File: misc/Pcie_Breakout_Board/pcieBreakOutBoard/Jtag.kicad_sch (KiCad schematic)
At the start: 6 parts, among them U1 FT2232HL, U3 93LCxxBxxOT

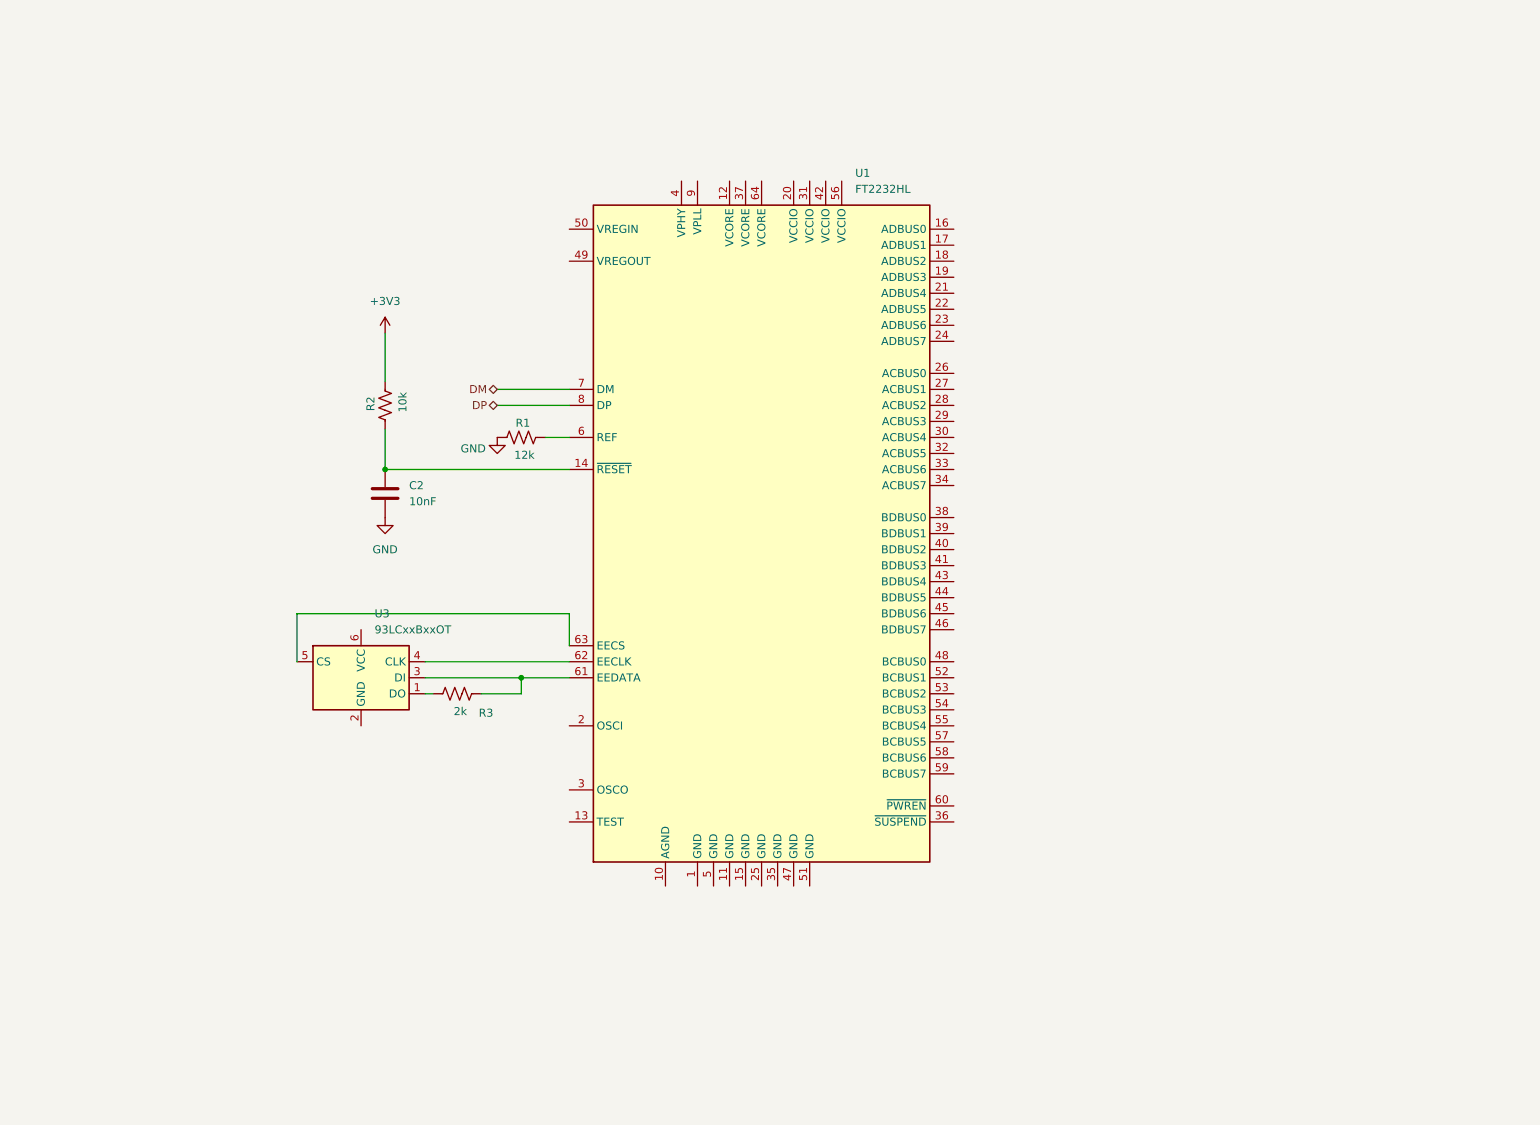
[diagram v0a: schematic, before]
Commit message: Jtag
Added jtag and serial interface to the breakout board
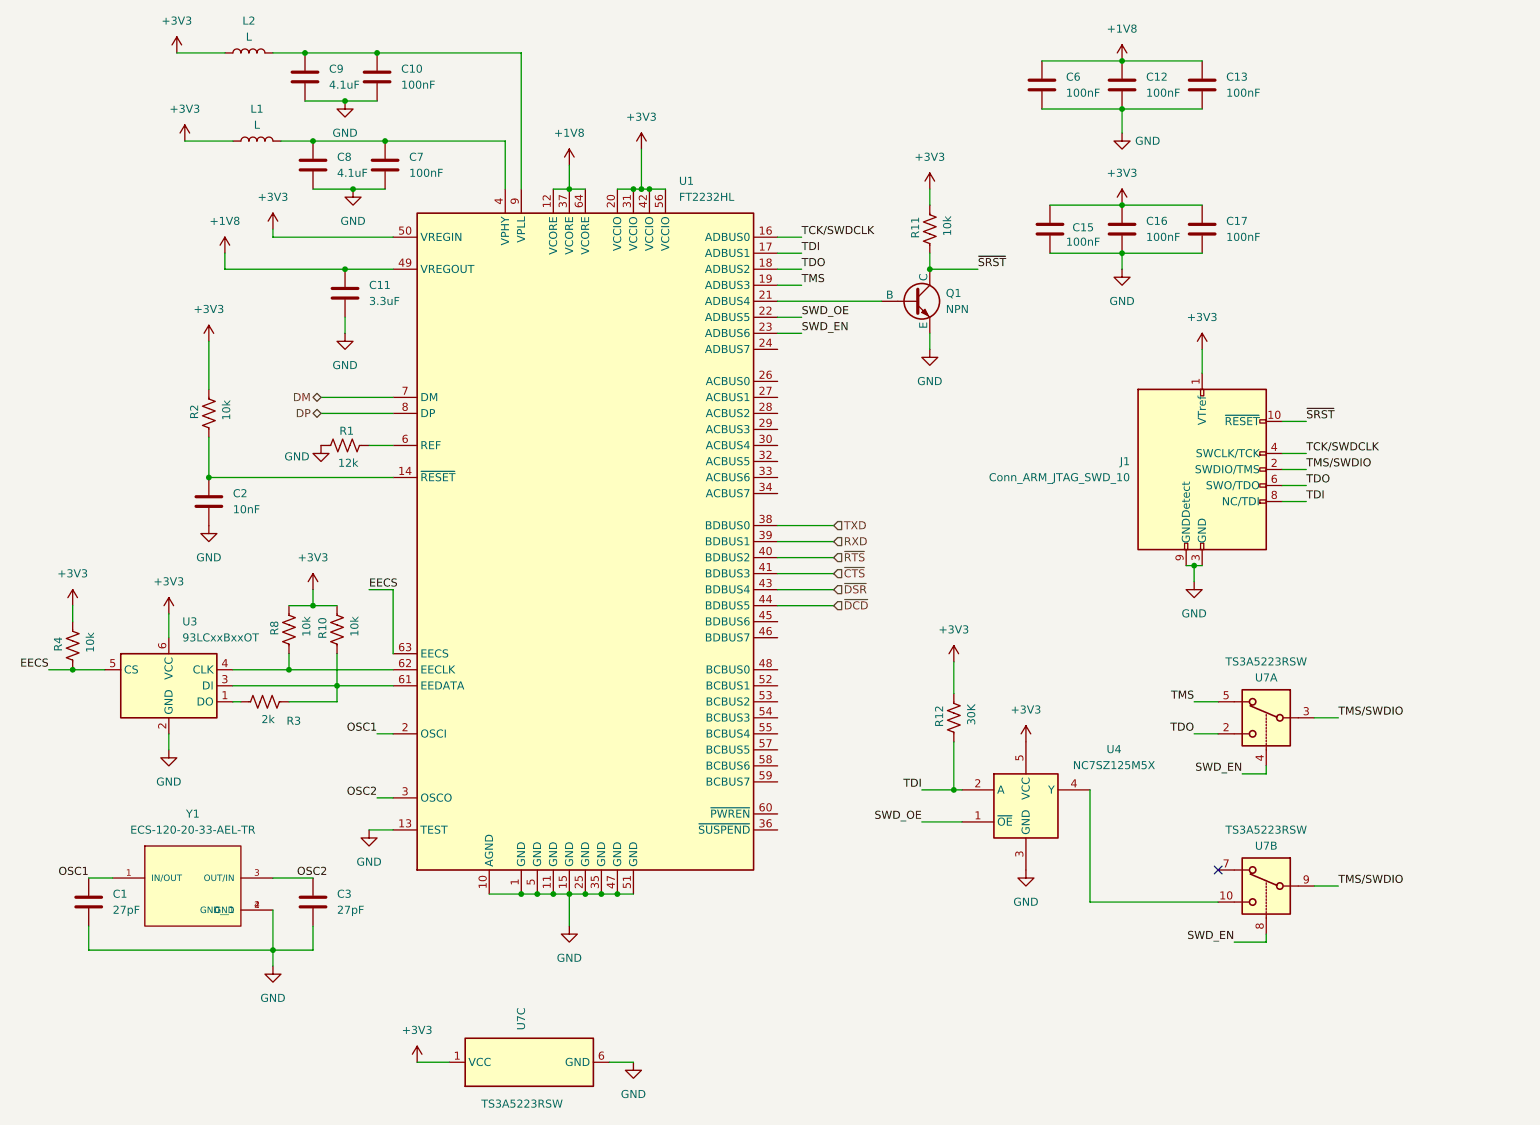
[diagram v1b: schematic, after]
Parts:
- added C1, C3: 27pF, Capacitor_SMD:C_0402_1005Metric_Pad0.74x0.62mm_HandSolder, symbol Device:C
- added C10, C12, C13, C15, C16, C17, C6, C7: 100nF, Capacitor_SMD:C_0402_1005Metric_Pad0.74x0.62mm_HandSolder, symbol Device:C
- added C11: 3.3uF, Capacitor_SMD:C_0402_1005Metric_Pad0.74x0.62mm_HandSolder, symbol Device:C
- added C8, C9: 4.1uF, Capacitor_SMD:C_0402_1005Metric_Pad0.74x0.62mm_HandSolder, symbol Device:C
- added J1: Conn_ARM_JTAG_SWD_10, Connector_PinHeader_1.27mm:PinHeader_2x05_P1.27mm_Vertical, symbol Connector:Conn_ARM_JTAG_SWD_10
- added L1, L2: L, Inductor_SMD:L_0402_1005Metric_Pad0.77x0.64mm_HandSolder, symbol Device:L
- added Q1: NPN, symbol Simulation_SPICE:NPN
- added R10, R11, R4, R8: 10k, Resistor_SMD:R_0402_1005Metric_Pad0.72x0.64mm_HandSolder, symbol Device:R_US
- added R12: 30K, Resistor_SMD:R_0402_1005Metric_Pad0.72x0.64mm_HandSolder, symbol Device:R_US
- added U4: NC7SZ125M5X, Package_TO_SOT_SMD:SOT-23-5, symbol 74xGxx:NC7SZ125M5X
- added U7: TS3A5223RSW, Package_DFN_QFN:Texas_RSW0010A_UQFN-10_1.4x1.8mm_P0.4mm, symbol Analog_Switch:TS3A5223RSW
- added Y1: ECS-120-20-33-AEL-TR, User_Footprint:XTAL_ECS-120-20-33-AEL-TR, symbol _Misc_Symbols:ECS-120-20-33-AEL-TR
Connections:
- net +3V3: now also U1.20 (VCCIO), U1.31 (VCCIO), U1.42 (VCCIO), U1.50 (VREGIN), U1.56 (VCCIO), U3.6 (VCC), C15.1, C16.1, C17.1, J1.1 (VTref), L1.1, L2.1, R10.2, R11.2, R12.2, R4.2, R8.2, U4.5 (VCC), U7.1 (VCC)
- net GND: now also U1.1 (GND), U1.10 (AGND), U1.11 (GND), U1.13 (TEST), U1.15 (GND), U1.25 (GND), U1.35 (GND), U1.47 (GND), U1.5 (GND), U1.51 (GND), U3.2 (GND), C1.2, C10.2, C11.2, C12.2, C13.2, C15.2, C16.2, C17.2, C3.2, C6.2, C7.2, C8.2, C9.2, J1.3 (GND), J1.5 (GND), J1.9 (GNDDetect), Q1.3 (E), U4.3 (GND), U7.6 (GND), Y1.2 (GND), Y1.4 (GND__1)
- net at R3.2, U1.61 (EEDATA), U3.3 (DI): now also R10.1
- net at U1.62 (EECLK), U3.4 (CLK): now also R8.1
- net EECS: now reaches U1.63 (EECS), U3.5 (CS)
- net EECS: now also R4.1
- net +1V8: now reaches U1.12 (VCORE)
- net +1V8: now also U1.37 (VCORE), U1.49 (VREGOUT), U1.64 (VCORE), C11.1, C12.1, C13.1, C6.1
- net TCK/SWDCLK: now reaches U1.16 (ADBUS0)
- net TCK/SWDCLK: now also J1.4 (SWCLK/TCK)
- net TDI: now reaches U1.17 (ADBUS1)
- net TDI: now also J1.8 (NC/TDI), R12.1, U4.2 (A)
- net TDO: now reaches U1.18 (ADBUS2)
- net TDO: now also J1.6 (SWO/TDO), U7.2
- net TMS: now reaches U1.19 (ADBUS3)
- net TMS: now also U7.5
- net OSC1: now reaches U1.2 (OSCI)
- net OSC1: now also C1.1, Y1.1 (IN/OUT)
- net at U1.21 (ADBUS4): now also Q1.2 (B)
- net SWD_OE: now reaches U1.22 (ADBUS5)
- net SWD_OE: now also U4.1 (~{OE})
- net SWD_EN: now reaches U1.23 (ADBUS6)
- net SWD_EN: now also U7.4, U7.8
- net OSC2: now reaches U1.3 (OSCO)
- net OSC2: now also C3.1, Y1.3 (OUT/IN)
- net TXD: now reaches U1.38 (BDBUS0)
- net RXD: now reaches U1.39 (BDBUS1)
- net at U1.4 (VPHY): now also C7.1, C8.1, L1.2
- net ~{RTS}: now reaches U1.40 (BDBUS2)
- net ~{CTS}: now reaches U1.41 (BDBUS3)
- net ~{DSR}: now reaches U1.43 (BDBUS4)
- net ~{DCD}: now reaches U1.44 (BDBUS5)
- net at U1.9 (VPLL): now also C10.1, C9.1, L2.2
- new net: U4.4 (Y), U7.10
- new net TMS/SWDIO: J1.2 (SWDIO/TMS), U7.3, U7.9
- new net ~{SRST}: J1.10 (~{RESET}), Q1.1 (C), R11.1
- no-connect marks 0 -> 1
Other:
- moved on the sheet: C2, R1, R2, R3, U1, U3

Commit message: routing
Start routing of the jtag part
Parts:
- removed Q1: NPN, symbol Simulation_SPICE:NPN
- added Q1: MMBT2222A, Package_TO_SOT_SMD:SOT-23_Handsoldering, symbol Transistor_BJT:MMBT2222A
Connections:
- net GND: now also Q1.2 (E)
- net OSC1: now also C3.1, Y1.3 (OUT/IN); no longer C1.1, Y1.1 (IN/OUT)
- net OSC2: now also C1.1, Y1.1 (IN/OUT); no longer C3.1, Y1.3 (OUT/IN)
- net ~{SRST}: now also Q1.3 (C)
- net at U1.21 (ADBUS4): now also Q1.1 (B)
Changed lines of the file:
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@@
 	)
 	(junction
-		(at 175.26 55.88)
-		(diameter 0)
-		(color 0 0 0 0)
-	)
-	(junction
 		(at 77.47 109.22)
 		(diameter 0)
@@
 	)
 	(junction
+		(at 175.26 55.88)
+		(diameter 0)
+		(color 0 0 0 0)
+	)
+	(junction
 		(at 179.07 138.43)
 		(diameter 0)
@@
 	)
 	(label "OSC2"
-		(at 74.93 152.4 0)
+		(at 41.91 152.4 0)
 		(effects
 			(font
@@
 	)
 	(label "OSC1"
-		(at 41.91 152.4 180)
+		(at 77.47 152.4 180)
 		(effects
 			(font
@@
 	)
 	(symbol
-		(lib_id "Simulation_SPICE:NPN")
-		(at 172.72 60.96 0)
-		(unit 1)
-		(exclude_from_sim no)
-		(in_bom yes)
-		(on_board yes)
-		(dnp no)
-		(fields_autoplaced yes)
-		(property "Reference" "Q1"
-			(at 177.8 59.6899 0)
-			(effects
-				(font
-					(size 1.27 1.27)
-				)
-				(justify left)
-			)
-		)
-		(property "Value" "NPN"
-			(at 177.8 62.2299 0)
-			(effects
-				(font
-					(size 1.27 1.27)
-				)
-				(justify left)
-			)
-		)
-		(property "Footprint" ""
-			(at 236.22 60.96 0)
-			(effects
-				(font
-					(size 1.27 1.27)
-				)
-				(hide yes)
-			)
-		)
-		(property "Datasheet" "https://ngspice.sourceforge.io/docs/ngspice-html-manual/manual.xhtml#cha_BJTs"
-			(at 236.22 60.96 0)
-			(effects
-				(font
-					(size 1.27 1.27)
-				)
-				(hide yes)
-			)
-		)
-		(property "Description" "Bipolar transistor symbol for simulation only, substrate tied to the emitter"
-			(at 172.72 60.96 0)
-			(effects
-				(font
-					(size 1.27 1.27)
-				)
-				(hide yes)
-			)
-		)
-		(property "Sim.Device" "NPN"
-			(at 172.72 60.96 0)
-			(effects
-				(font
-					(size 1.27 1.27)
-				)
-				(hide yes)
-			)
-		)
-		(property "Sim.Type" "GUMMELPOON"
-			(at 172.72 60.96 0)
-			(effects
-				(font
-					(size 1.27 1.27)
-				)
-				(hide yes)
-			)
-		)
-		(property "Sim.Pins" "1=C 2=B 3=E"
-			(at 172.72 60.96 0)
-			(effects
-				(font
-					(size 1.27 1.27)
-				)
-				(hide yes)
-			)
-		)
-		(pin "1"
-		)
-		(pin "2"
-		)
-		(pin "3"
-		)
-		(instances
-			(project "pcieBreakOutBoard"
-				(path "/12b1338c-66b4-40fc-bcb6-22ba3c1b4efc/a6f2494a-799a-42fc-83bb-1a352a63812f"
-					(reference "Q1")
-					(unit 1)
-				)
-			)
-		)
-	)
-	(symbol
 		(lib_id "Device:R_US")
 		(at 60.96 78.74 180)
@@
 					(unit 1)
 				)
+			)
+		)
+	)
+	(symbol
+		(lib_id "Transistor_BJT:MMBT2222A")
+		(at 172.72 60.96 0)
+		(unit 1)
+		(exclude_from_sim no)
+		(in_bom yes)
+		(on_board yes)
+		(dnp no)
+		(fields_autoplaced yes)
+		(property "Reference" "Q1"
+			(at 177.8 59.6899 0)
+			(effects
+				(font
+					(size 1.27 1.27)
+				)
+				(justify left)
+			)
+		)
+		(property "Value" "MMBT2222A"
+			(at 177.8 62.2299 0)
+			(effects
+				(font
+					(size 1.27 1.27)
+				)
+				(justify left)
+			)
+		)
+		(property "Footprint" "Package_TO_SOT_SMD:SOT-23_Handsoldering"
+			(at 177.8 62.865 0)
+			(effects
+				(font
+					(size 1.27 1.27)
+					(italic yes)
+				)
+				(justify left)
+				(hide yes)
+			)
+		)
+		(property "Datasheet" "https://assets.nexperia.com/documents/data-sheet/MMBT2222A.pdf"
+			(at 172.72 60.96 0)
+			(effects
+				(font
+					(size 1.27 1.27)
+				)
+				(justify left)
+				(hide yes)
+			)
+		)
+		(property "Description" "600mA Ic, 40V Vce, NPN Transistor, SOT-23"
+			(at 172.72 60.96 0)
+			(effects
+				(font
+					(size 1.27 1.27)
+				)
+				(hide yes)
+			)
+		)
+		(property "Sim.Device" "NPN"
+			(at 172.72 60.96 0)
+			(effects
+				(font
+					(size 1.27 1.27)
+				)
+				(hide yes)
+			)
+		)
+		(property "Sim.Pins" "1=B 2=E 3=C"
+			(at 172.72 60.96 0)
+			(effects
+				(font
+					(size 1.27 1.27)
+				)
+				(hide yes)
+			)
+		)
+		(pin "2"
+		)
+		(pin "3"
+		)
+		(pin "1"
+		)
+		(instances
+			(project "pcieBreakOutBoard"
+				(path "/12b1338c-66b4-40fc-bcb6-22ba3c1b4efc/a6f2494a-799a-42fc-83bb-1a352a63812f"
+					(reference "Q1")
+					(unit 1)
+				)

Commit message: layout
finished 70% of layout
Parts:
- added J4: Conn_02x04_Odd_Even, Connector_PinHeader_2.54mm:PinHeader_2x04_P2.54mm_Vertical, symbol Connector_Generic:Conn_02x04_Odd_Even
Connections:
- net GND: now also J4.6 (Pin_6), J4.8 (Pin_8)
- net RXD: now also J4.4 (Pin_4)
- net TXD: now also J4.2 (Pin_2)
- net ~{CTS}: now also J4.3 (Pin_3)
- net ~{DCD}: now also J4.7 (Pin_7)
- net ~{DSR}: now also J4.5 (Pin_5)
- net ~{RTS}: now also J4.1 (Pin_1)
